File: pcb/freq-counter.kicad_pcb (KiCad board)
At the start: 4 copper layers, 152.4 x 167.6 mm, 103 parts, among them J1 RPM on board, J10 Power_T1, J2 BNC, J3 RPM to Board, J4 Jack-DC, J5 Segments-Terminal0, J6 Digits-Terminal0, J7 Segments-Terminal1, J8 Digits-Terminal1, J9 Power_Terminal1, Q1 CSC388A, Q10 2SC1815, Q11 2SC1815, Q12 2SC1815, Q13 2SC1815, Q14 2SC1815, Q2 CSC388A, Q3 2SA1015, Q4 2SC1815, Q5 2SC1815, Q6 CSC388A, Q7 CSC388A, Q8 CSC388A, Q9 2SC1815, SW1 on/off, SW2 count up, SW3 toggle, SW4 SW_SIGNAL, U1 SN74HC02N, U2 ATTINY4313-PU(freq-counter), U3 EE-SX460, U4 74HC00, U5 74HC00, U6 74HC00, U7 7seg-2digit-ca, U8 7seg-2digit-ca, U9 7seg-2digit-ca, Y1 10MHz

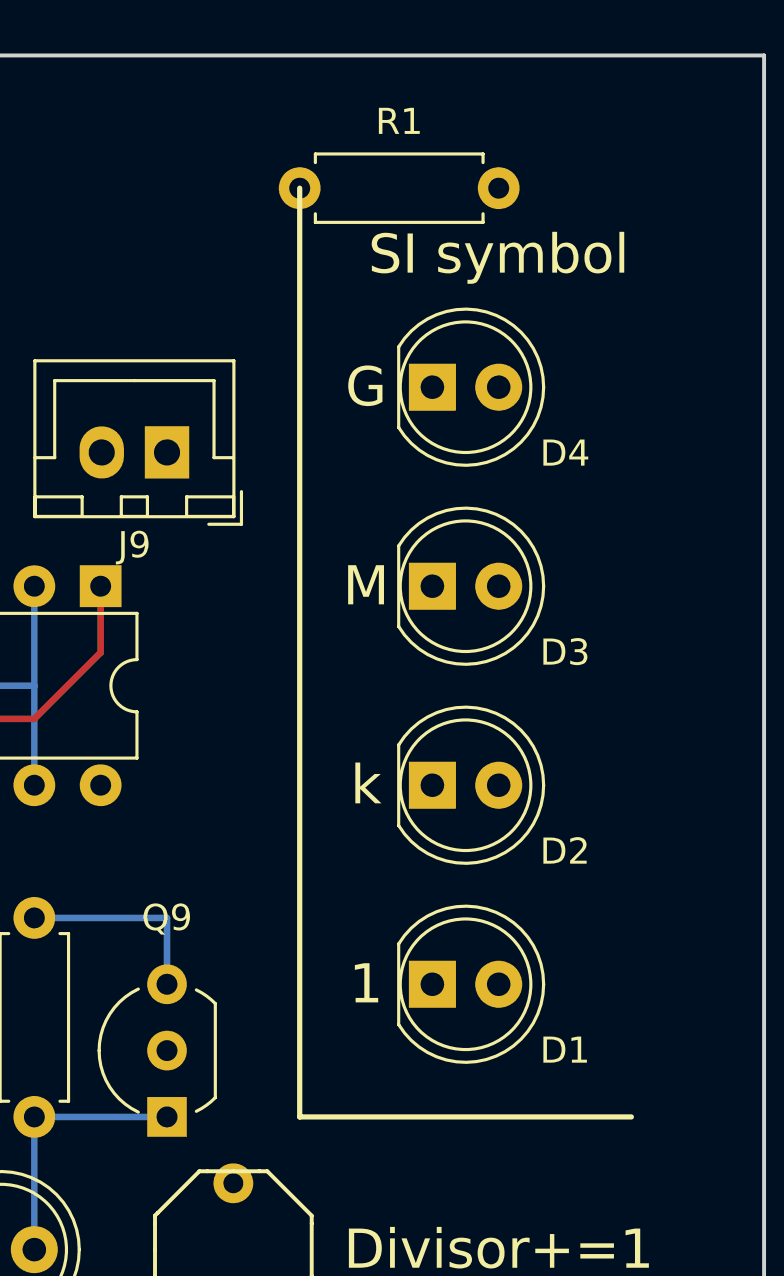
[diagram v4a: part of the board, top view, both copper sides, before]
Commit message: 1kMGの電流制限抵抗(R1)の配置を水平から垂直に変更。
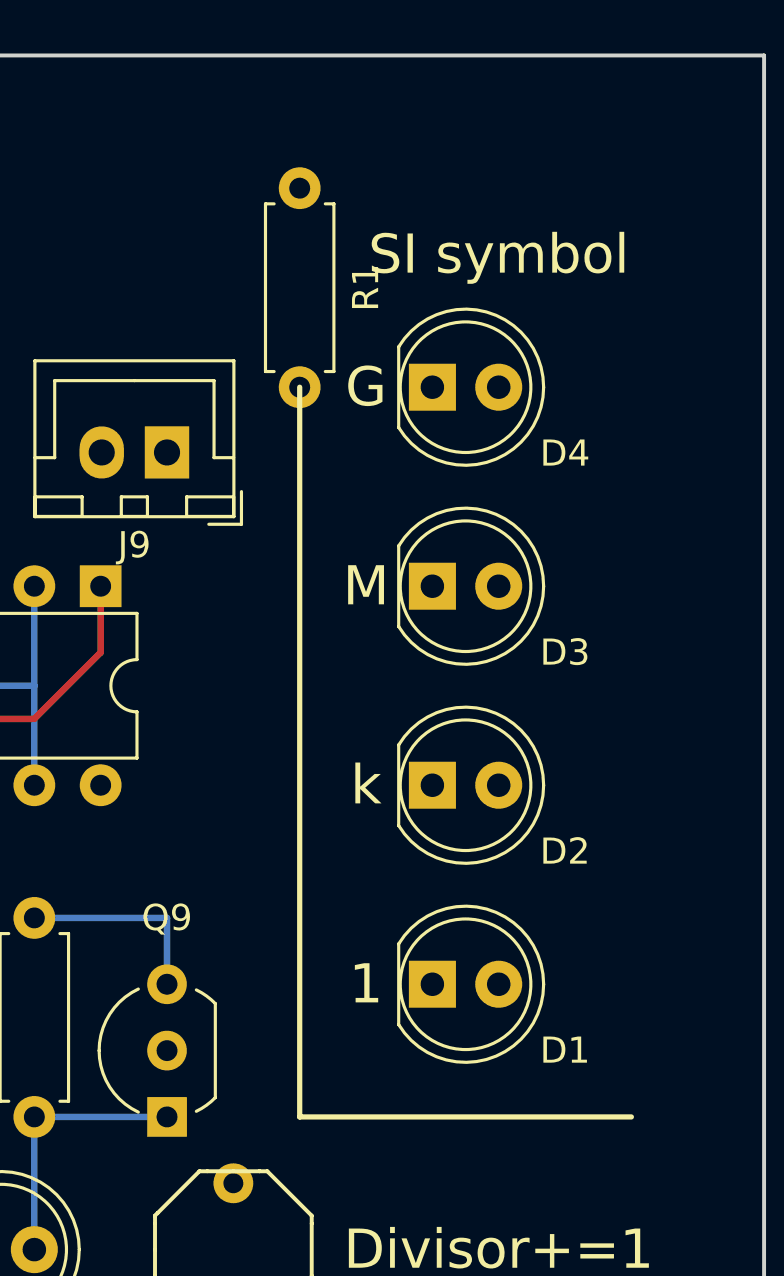
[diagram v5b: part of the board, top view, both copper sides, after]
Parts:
- moved R1 10.8 mm to (162.6, 43.2), turned to 90 degrees
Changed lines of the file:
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@@
   )
   (module Resistors_THT:R_Axial_DIN0207_L6.3mm_D2.5mm_P7.62mm_Horizontal (layer F.Cu)
-    (at 170.18 35.56 180)
+    (at 162.56 43.18 90)
     (descr "Resistor, Axial_DIN0207 series, Axial, Horizontal, pin pitch=7.62mm, 0.25W = 1/4W, length*diameter=6.3*2.5mm^2, http://cdn-reichelt.de/documents/datenblatt/B400/1_4W%23YAG.pdf")
     (tags "Resistor Axial_DIN0207 series Axial Horizontal pin pitch 7.62mm 0.25W = 1/4W length 6.3mm diameter 2.5mm")
-    (fp_text reference R1 (at 3.809998 2.540007 180) (layer F.SilkS)
+    (fp_text reference R1 (at 3.809998 2.540007 90) (layer F.SilkS)
       (effects (font (size 1 1) (thickness 0.15)))
     )
-    (fp_text value 470 (at 3.809998 0.000007 180) (layer F.Fab)
+    (fp_text value 470 (at 3.809998 0.000007 90) (layer F.Fab)
       (effects (font (size 1 1) (thickness 0.15)))
     )
@@
     (fp_line (start 8.7 1.6) (end 8.7 -1.6) (layer F.CrtYd) (width 0.05))
     (fp_line (start 8.7 -1.6) (end -1.05 -1.6) (layer F.CrtYd) (width 0.05))
-    (pad 1 thru_hole circle (at 0 0 180) (size 1.6 1.6) (drill 0.8) (layers *.Cu *.Mask)
+    (pad 1 thru_hole circle (at 0 0 90) (size 1.6 1.6) (drill 0.8) (layers *.Cu *.Mask)
       (net 6 "Net-(D1-Pad1)"))
-    (pad 2 thru_hole oval (at 7.62 0 180) (size 1.6 1.6) (drill 0.8) (layers *.Cu *.Mask)
+    (pad 2 thru_hole oval (at 7.62 0 90) (size 1.6 1.6) (drill 0.8) (layers *.Cu *.Mask)
       (net 95 GND))
     (model ${KISYS3DMOD}/Resistors_THT.3dshapes/R_Axial_DIN0207_L6.3mm_D2.5mm_P7.62mm_Horizontal.wrl
@@
     (effects (font (size 1.5 1.5) (thickness 0.3)))
   )
-  (gr_line (start 162.56 71.12) (end 162.56 35.56) (layer F.SilkS) (width 0.2))
+  (gr_line (start 162.56 71.12) (end 162.56 43.18) (layer F.SilkS) (width 0.2))
   (gr_text 4 (at 118.109994 80.644984 360) (layer F.SilkS)
     (effects (font (size 1.5 1.5) (thickness 0.3)))

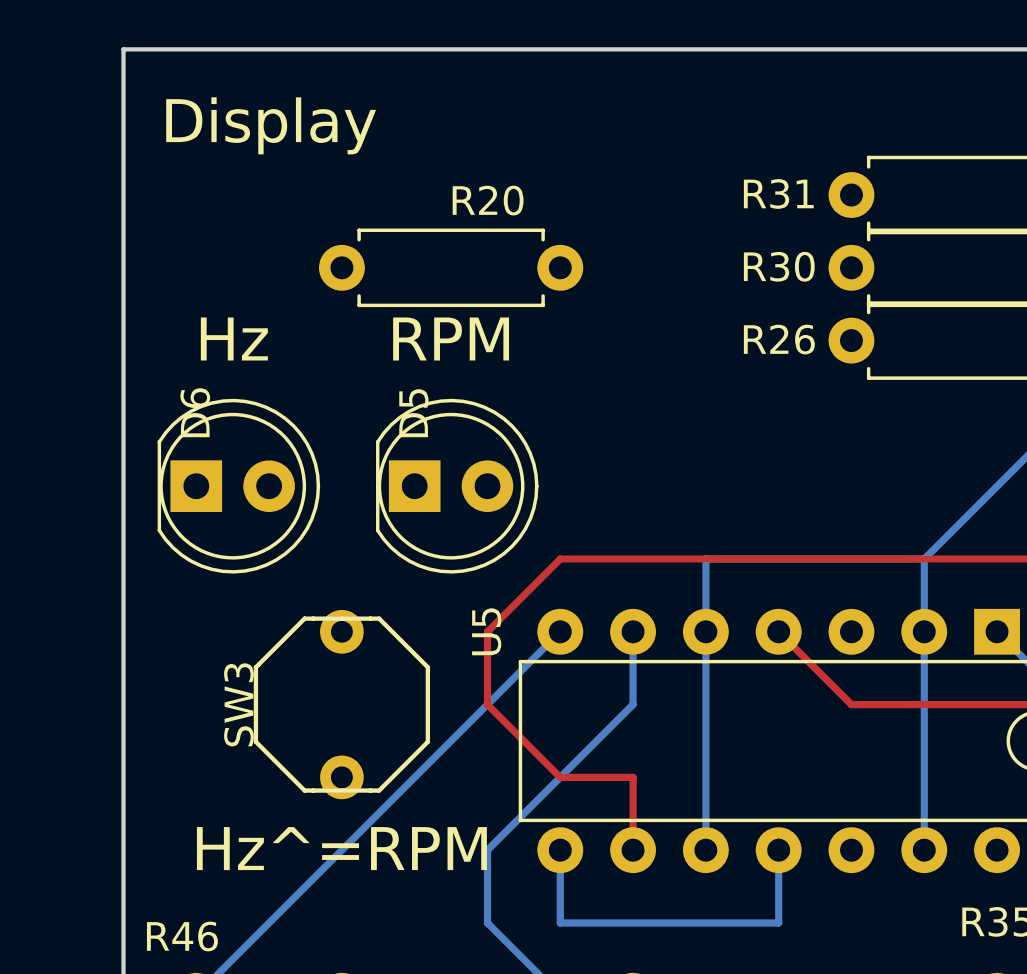
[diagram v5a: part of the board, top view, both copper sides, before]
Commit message: Display部の Hz/RPM をTerminal接続にした。
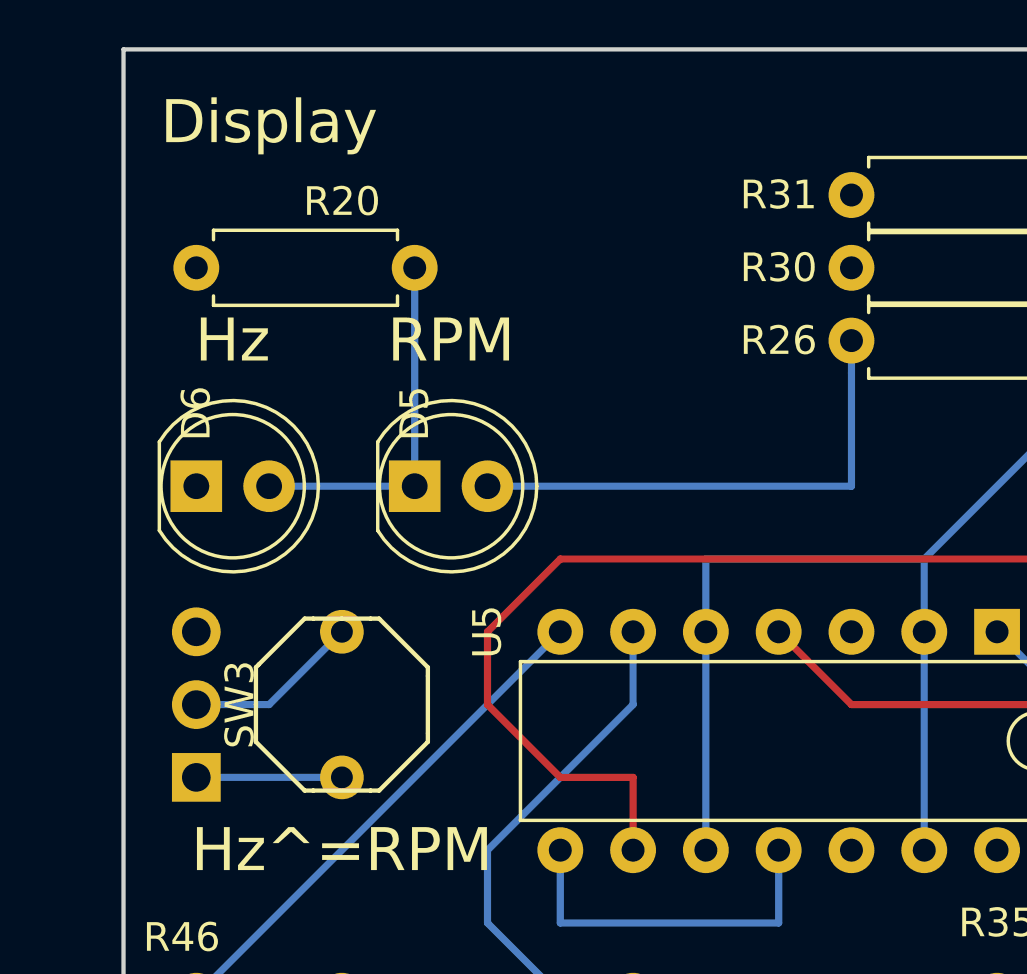
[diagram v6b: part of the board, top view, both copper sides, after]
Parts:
- added J11: Hz/RPM_Terminal, Conn_PinHeader_2.54mm:PinHeader_1x03_P2.54mm_Vertical, B.Cu at (86.4, 55.9)
- moved R20 5.08 mm to (86.4, 38.1)
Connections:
- D5 pad 2: VCC -> VCC_T1
- D6 pad 1: GND -> GND_T1
- R20 pad 1: Net-(D5-Pad1) -> /Hz/RPM_T1
- R20 pad 2: /Hz/RPM -> Net-(D5-Pad1)
- SW3 pad 1: Net-(C7-Pad1) -> /TOGGLE_0
- SW3 pad 2: Net-(C9-Pad2) -> /TOGGLE_1
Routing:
- net (no net): track 17.8 -> 61.0 mm
- net Net-(D1-Pad1): track 27.9 -> 0.00 mm
- net VCC_T1: track 130.6 -> 148.4 mm
- net GND_T1: track 119.3 -> 133.8 mm
- net /Hz/RPM_T1: track 0.00 -> 13.7 mm
- net /TOGGLE_1: track 0.00 -> 6.13 mm
- net /TOGGLE_0: track 0.00 -> 5.08 mm
- net Net-(D5-Pad1): track 15.2 -> 12.7 mm

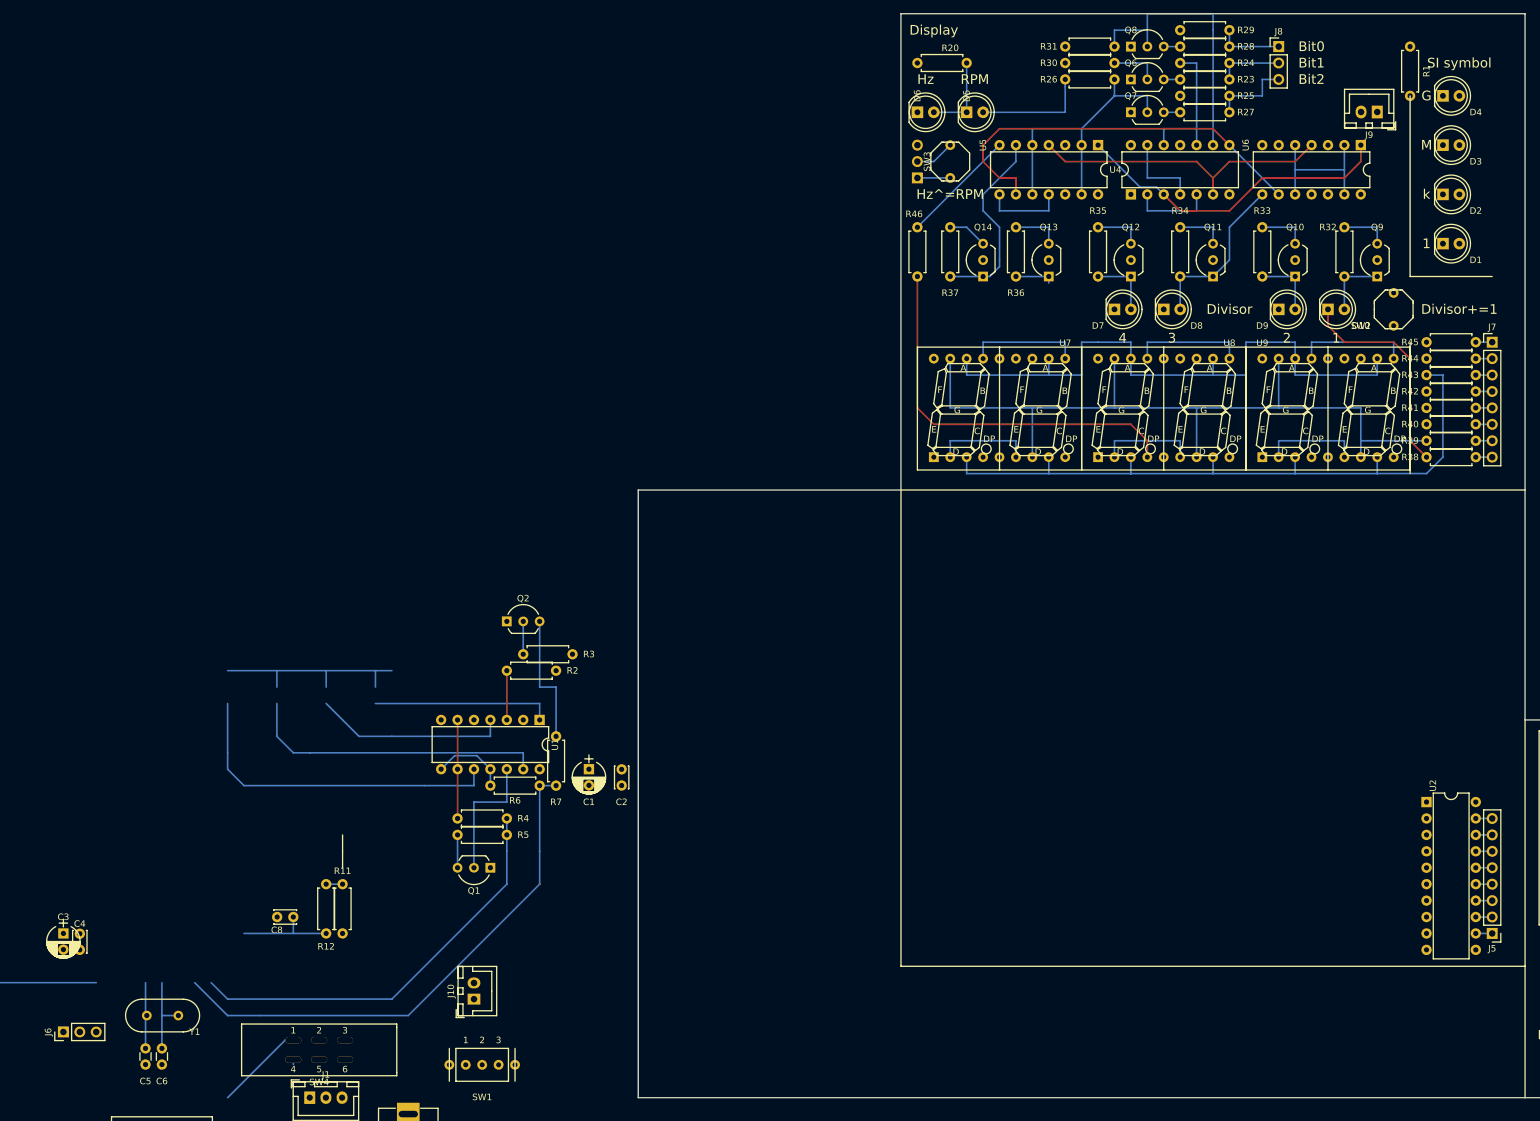
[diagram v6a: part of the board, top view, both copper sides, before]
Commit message: Hz/RPM のterminal化が完成。
他にもpackages3dの設定や，footprintの設定を変えたりするなど。
余計な手間を掛けていると思える。
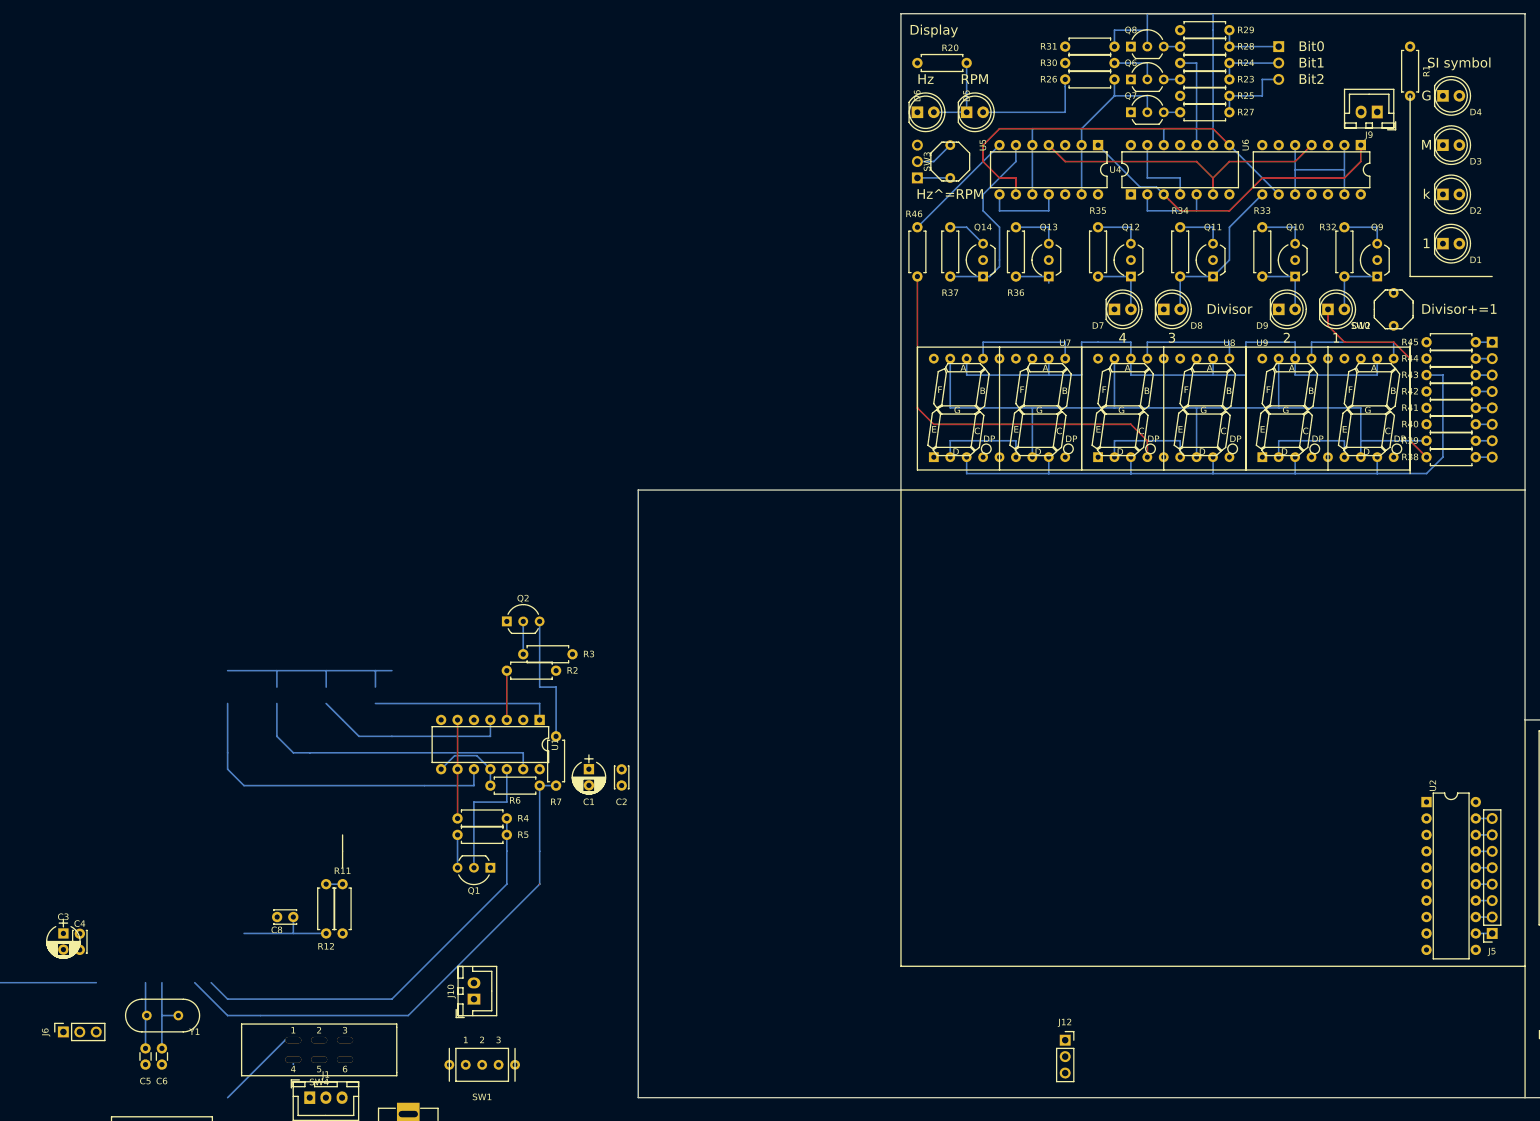
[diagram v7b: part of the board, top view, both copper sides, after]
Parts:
- added J12: Hz/RPM_Terminal0, Connector_PinSocket_2.54mm:PinSocket_1x03_P2.54mm_Vertical, F.Cu at (109.2, 189.2)
- J11: value Hz/RPM_Terminal -> Hz/RPM_Terminal1; footprint Conn_PinHeader_2.54mm:PinHeader_1x03_P2.54mm_Vertical -> Connector_PinHeader_2.54mm:PinHeader_1x03_P2.54mm_Vertical
- J5: footprint Conn_PinHeader_2.54mm:PinHeader_1x08_P2.54mm_Vertical -> Connector_PinSocket_2.54mm:PinSocket_1x08_P2.54mm_Vertical
- J6: footprint Conn_PinHeader_2.54mm:PinHeader_1x03_P2.54mm_Vertical -> Connector_PinSocket_2.54mm:PinSocket_1x03_P2.54mm_Vertical
- J7: footprint Conn_PinHeader_2.54mm:PinHeader_1x08_P2.54mm_Vertical -> Connector_PinHeader_2.54mm:PinHeader_1x08_P2.54mm_Vertical; moved to B.Cu
- J8: footprint Conn_PinHeader_2.54mm:PinHeader_1x03_P2.54mm_Vertical -> Connector_PinHeader_2.54mm:PinHeader_1x03_P2.54mm_Vertical; moved to B.Cu
- turned J7 to 180 degrees
- turned J8 to 180 degrees
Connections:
- net /Hz/RPM renamed /Hz/RPM_T0
- net /TOGGLE_0 renamed /TOGGLE0_T1
- net /TOGGLE_1 renamed /TOGGLE1_T1
- net Net-(C7-Pad1) renamed /TOGGLE0_T0
- net Net-(C9-Pad2) renamed /TOGGLE1_T0
